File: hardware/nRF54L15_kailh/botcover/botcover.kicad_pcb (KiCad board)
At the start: 2 copper layers, 328.1 x 198.6 mm, 121 parts

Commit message: M  hardware/nRF54L15_kailh/botcover/botcover.kicad_pcb
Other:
- board text added: "NOTE: - Use FreeCAD to generate STEP file to preserve Bezier curves. KiCad facets the Bezier curves. - Do not include hexagons in edge_cuts since FreeCAD fails trying to deal with many lines. Import the step file into Fusion, along with dxf of Layer which contains hexagons. Cut hexagons and countersink holes"
- board text removed: "NOTE: - Use FreeCAD to generate STEP file to preserve Bezier curves. KiCad facets the Bezier curves."
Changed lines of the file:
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@@
 		(layer "User.6")
 	)
-	(gr_text "NOTE: \n- Use FreeCAD to generate STEP file to preserve Bezier curves.\n  KiCad facets the Bezier curves."
+	(gr_text "NOTE: \n- Use FreeCAD to generate STEP file to preserve Bezier curves.\n  KiCad facets the Bezier curves.\n- Do not include hexagons in edge_cuts since FreeCAD fails trying\n  to deal with many lines. Import the step file into Fusion, along\n  with dxf of Layer which contains hexagons. Cut hexagons and countersink holes"
 		(at 81.13 154.65 0)
 		(layer "F.Fab")

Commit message: M  .gitignore A  hardware/nRF54L15_gateron_kailh_TMR2615/LED.kicad_sch A  hardware/nRF54L15_gateron_kailh_TMR2615/fp-lib-table A  hardware/nRF54L15_gateron_kailh_TMR2615/nRF54L15_gateron_kailh_TMR2615.kicad_pcb A  hardware/nRF54L15_gateron_kailh_TMR2615/nRF54L15_gateron_kailh_TMR2615.kicad_prl A  hardware/nRF54L15_gateron_kailh_TMR2615/nRF54L15_gateron_kailh_TMR2615.kicad_pro A  hardware/nRF54L15_gateron_kailh_TMR2615/nRF54L15_gateron_kailh_TMR2615.kicad_sch A  hardware/nRF54L15_gateron_kailh_TMR2615/pcb-eagle-import.kicad_sym A  hardware/nRF54L15_gateron_kailh_TMR2615/switch.kicad_sch A  hardware/nRF54L15_gateron_kailh_TMR2615/sym-lib-table M  hardware/nRF54L15_kailh/border.py A  hardware/nRF54L15_kailh/botcase/botcase-Edge_Cuts.pdf M  hardware/nRF54L15_kailh/botcase/botcase.kicad_pcb M  hardware/nRF54L15_kailh/botcase/botcase.kicad_sch M  hardware/nRF54L15_kailh/botcover/botcover.kicad_pcb M  hardware/nRF54L15_kailh/botcover/botcover.kicad_sch M  hardware/nRF54L15_kailh/placefp.py A  hardware/nRF54L15_kailh/rebuild_board.py A  hardware/nRF54L15_kailh/run.sh M  hardware/nRF54L15_kailh/swplate/swplate.kicad_pcb M  hardware/nRF54L15_kailh/swplate/swplate.kicad_sch A  hardware/nRF54L15_kailh/tmr-footprints/Kailh_gateron_sw_lowpro.kicad_mod M  hardware/nRF54L15_kailh/tmr-footprints/Kailh_sw_lowpro.kicad_mod A  hardware/nRF54L15_kailh/tmr-footprints/M1.4_tap.kicad_mod A  hardware/nRF54L15_kailh/tmr-footprints/M2.5_tap.kicad_mod A  hardware/nRF54L15_kailh/tmr-footprints/MountingHole_1.6mm_M1.4_NoPad.kicad_mod M  hardware/nRF54L15_kailh/topcase/topcase.kicad_pcb A  hardware/nRF54L15_kailh/wristrest/fp-lib-table A  hardware/nRF54L15_kailh/wristrest/sym-lib-table A  hardware/nRF54L15_kailh/wristrest/wristrest.kicad_pcb A  hardware/nRF54L15_kailh/wristrest/wristrest.kicad_prl A  hardware/nRF54L15_kailh/wristrest/wristrest.kicad_pro A  hardware/nRF54L15_kailh/wristrest/wristrest.kicad_sch
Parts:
- Hm1, Hm2, Hr1, Hr10, Hr11, Hr12, Hr13, Hr14, Hr15, Hr16, Hr17, Hr18, Hr19, Hr2, Hr20, Hr21, Hr22, Hr23, Hr24, Hr25, Hr26, Hr27, Hr28, Hr29, Hr3, Hr4, Hr5, Hr6, Hr7, Hr8, Hr9: footprint tmr-lib:MountingHole_1.5mm_M1.4_NoPad -> tmr-lib:MountingHole_1.6mm_M1.4_NoPad

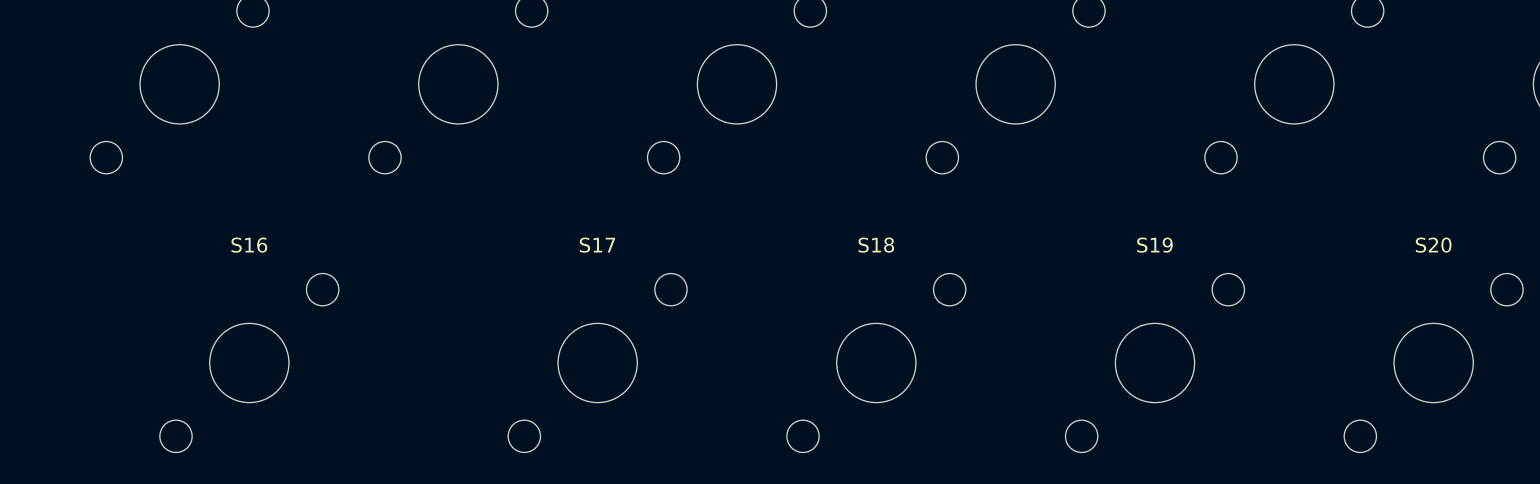
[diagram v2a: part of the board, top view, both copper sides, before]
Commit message: M  hardware/nRF54L15_kailh/border.py M  hardware/nRF54L15_kailh/botcover/botcover.kicad_pcb M  hardware/nRF54L15_kailh/botcover/botcover.kicad_sch M  hardware/nRF54L15_kailh/placefp.py A  hardware/nRF54L15_kailh/tmr-footprints/Aliexpress_SW_TACT_4x4x1.5mm_hole_only.kicad_mod
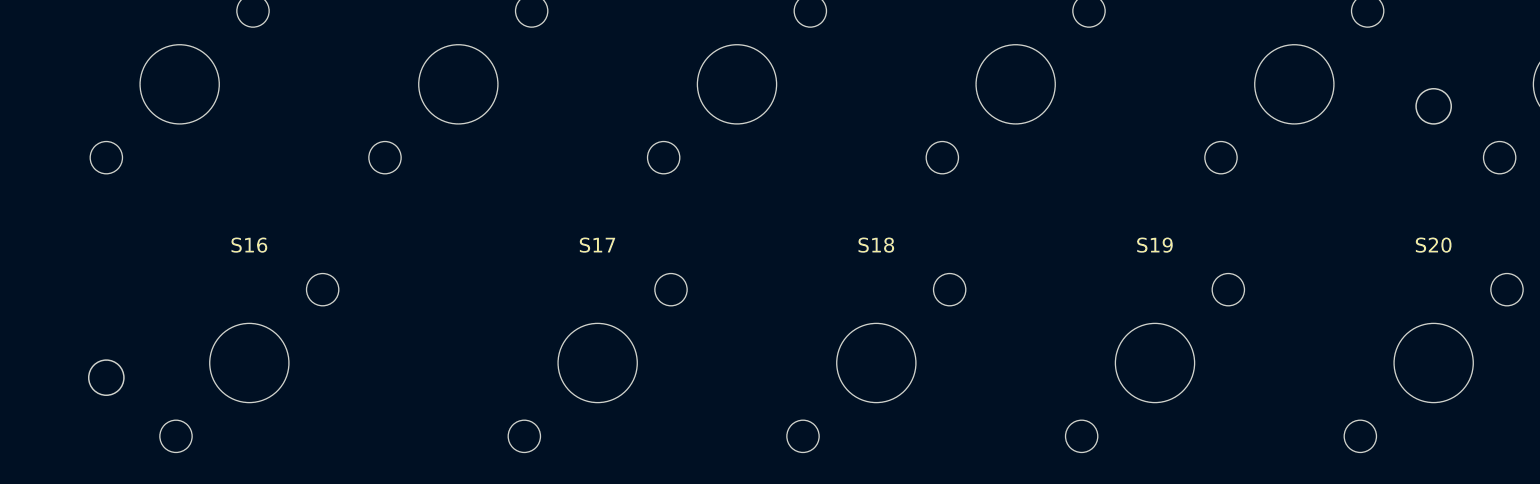
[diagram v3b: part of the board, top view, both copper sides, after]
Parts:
- added SW1: SW_DIP_x01, tmr-lib:Aliexpress_SW_TACT_4x4x1.5mm_hole_only, B.Cu at (104.5, 1.50)
- added SW2: SW_DIP_x01, tmr-lib:Aliexpress_SW_TACT_4x4x1.5mm_hole_only, B.Cu at (14.0, 20.0)
